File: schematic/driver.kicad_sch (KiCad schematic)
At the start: 14 parts, among them U2 PC817, U3 BUK9K52-60E, U4 BUK9K52-60E, U6 PC817, U7 PC817, U8 PC817

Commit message: a
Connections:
- net Vdrive: now also U2.4
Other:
- title: (none) -> Peltier Driver
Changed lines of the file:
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@@
 (kicad_sch (version 20211123) (generator eeschema)
   (paper "A4")
+  (title_block
+    (title "Peltier Driver")
+    (date "2022-03-18")
+    (comment 1 "Engineer/Draftsman: Joesphan Lu")
+  )
   (junction (at 154.94 57.15) (diameter 0) (color 0 0 0 0)
   )
@@
     (stroke (width 0) (type default) (color 0 0 0 0))
   )
-  (wire (pts (xy 120.65 77.47) (xy 120.65 80.01))
+  (wire (pts (xy 120.65 74.93) (xy 120.65 80.01))
     (stroke (width 0) (type default) (color 0 0 0 0))
   )
@@
     (pin "2")
   )
+  (symbol (lib_id "power:Vdrive") (at 120.65 74.93 0) (mirror y) (unit 1)
+    (in_bom yes) (on_board yes) (fields_autoplaced)
+    (property "Reference" "#PWR?" (id 0) (at 125.73 78.74 0)
+      (effects (font (size 1.27 1.27)) hide)
+    )
+    (property "Value" "Vdrive" (id 1) (at 120.65 71.3542 0))
+    (property "Footprint" "" (id 2) (at 120.65 74.93 0)
+      (effects (font (size 1.27 1.27)) hide)
+    )
+    (property "Datasheet" "" (id 3) (at 120.65 74.93 0)
+      (effects (font (size 1.27 1.27)) hide)
+    )
+    (pin "1")
+  )
   (symbol (lib_id "Device:R") (at 97.79 99.06 270) (unit 1)

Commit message: e
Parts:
- removed C11, C9: 10uF, Capacitor_SMD:C_0805_2012Metric_Pad1.18x1.45mm_HandSolder, symbol Device:C
- removed D1, D2: LL4148, Diode_SMD:D_MiniMELF, symbol Diode:LL4148
- removed R10, R2, R3: 300, Resistor_SMD:R_0805_2012Metric_Pad1.20x1.40mm_HandSolder, symbol Device:R
- removed U2, U6, U7: PC817, Package_SO:SOP-4_3.8x4.1mm_P2.54mm, symbol Isolator:PC817
- added D?: ZMM3V9, Diode_SMD:D_MiniMELF, symbol Diode:ZMMxx
- added R? (x2): 300, Resistor_SMD:R_0805_2012Metric_Pad1.20x1.40mm_HandSolder, symbol Device:R
- added U? (x2): PC817, Package_DIP:DIP-4_W7.62mm, symbol Isolator:PC817
- added U? (x3): NL17SZ14, Package_TO_SOT_SMD:SOT-553, symbol 1KicadLib:NL17SZ14
- added U?: slg55021, symbol 1KicadLib:slg55021
- U8: footprint Package_SO:SOP-4_3.8x4.1mm_P2.54mm -> Package_DIP:DIP-4_W7.62mm
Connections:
- net DRIVER_N: now also R?.2
- net GND: now also U?.2, U?.2, U?.4 (GND)
- net PELTIER_P: now also U?.6 (S)
- net VCC: now also U?.5 (D)
- net Vdrive: now also U?.4, U?.4
- net at U3.4 (G): now also U?.4 (Y)
- net at U3.2 (G): now also D?.2 (A)
- new net: R?.1, U?.1 (x2)
- new net: D?.1 (K), U?.7 (G)
- new net +5V: U?.1 (VCC)
- new net S1_PG: U?.8 (PG)
- new net ~DRIVER_DIR: U?.2 (A), U?.2 (A), U?.2 (ON)
- new net ~DRIVER_EN: U?.3 (SHDN#)

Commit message: d
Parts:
- removed R11, R? (x2): 300, Resistor_SMD:R_0805_2012Metric_Pad1.20x1.40mm_HandSolder, symbol Device:R
- removed U8, U? (x2): PC817, Package_DIP:DIP-4_W7.62mm, symbol Isolator:PC817
- added D2: (no value), Diode_SMD:D_MiniMELF, symbol Diode:ZMMxx
- added J1: (no value), symbol Connector:Conn_01x02_Female
- added U18: (no value), 1kicadlib:TDFN_8_2x2mm_EP_0.9x1.65mm, symbol 1KicadLib:slg55021
- D1: renamed from D?; value ZMM3V9 -> (none)
- U2, U7, U8: renamed from U?; value NL17SZ14 -> (none)
- U3, U4: value BUK9K52-60E -> (none); footprint 1KicadLib:LFPAK56D -> (none); symbol schematic-rescue:BUK9K52-60E-1KicadLib -> 1KicadLib:BUK9K52-60E
- U6: renamed from U?; value slg55021 -> (none); footprint (none) -> 1kicadlib:TDFN_8_2x2mm_EP_0.9x1.65mm
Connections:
- net +5V: now also U2.5 (VCC), U7.5 (VCC), U8.5 (VCC), U18.1 (VCC)
- net GND: now also U2.3 (GND), U7.3 (GND), U8.3 (GND), U18.4 (GND)
- net VCC: now also U18.5 (D)
- net ~DRIVER_EN: now also U18.3 (SHDN#)
- net at U4.4 (G): now also U8.2 (A)
- net at U4.2 (G): now also D2.2 (A)
- net at U8.4 (Y): now also U7.4 (Y), U18.2 (ON)
- net PELTIER_N: no longer names the net of U4.1 (S), U4.5 (D), U4.6 (D)
- net PELTIER_N: now also J1.1 (Pin_1), U18.6 (S)
- net PELTIER_P: no longer names the net of U3.1 (S), U3.5 (D), U3.6 (D), U6.6 (S)
- net PELTIER_P: now also J1.2 (Pin_2)
- net S1_PG: no longer names the net of U6.8 (PG)
- new net: D2.1 (K), U18.7 (G)
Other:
- moved on the sheet: U2, U7, U8

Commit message: d
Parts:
- D1, D2: value (none) -> ZMM3V9
- J1: value (none) -> Peltier Connection; footprint (none) -> Connector_PinHeader_2.54mm:PinHeader_1x02_P2.54mm_Vertical
- U18, U6: value (none) -> slg55021; footprint 1kicadlib:TDFN_8_2x2mm_EP_0.9x1.65mm -> 1KicadLib:TDFN_8_2x2mm_EP_0.9x1.65mm
- U2, U7, U8: value (none) -> NL17SZ14
- U3, U4: value (none) -> BUK9K52-60E; footprint (none) -> 1KicadLib:LFPAK56D
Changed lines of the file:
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@@
       (effects (font (size 1.27 1.27)) (justify left))
     )
-    (property "Value" "" (id 1) (at 129.6416 109.728 0)
-      (effects (font (size 1.27 1.27)) (justify left))
-    )
-    (property "Footprint" "" (id 2) (at 127 107.95 0)
+    (property "Value" "BUK9K52-60E" (id 1) (at 129.6416 109.728 0)
+      (effects (font (size 1.27 1.27)) (justify left))
+    )
+    (property "Footprint" "1KicadLib:LFPAK56D" (id 2) (at 127 107.95 0)
       (effects (font (size 1.27 1.27)) hide)
     )
     (property "Datasheet" "" (id 3) (at 127 107.95 0)
+      (effects (font (size 1.27 1.27)) hide)
+    )
+    (pin "3")
+    (pin "4")
+    (pin "5")
+    (pin "6")
+  )
+  (symbol (lib_id "1KicadLib:BUK9K52-60E") (at 172.72 107.95 0) (mirror y) (unit 2)
+    (in_bom yes) (on_board yes)
+    (property "Reference" "U4" (id 0) (at 170.053 107.4166 0)
+      (effects (font (size 1.27 1.27)) (justify left))
+    )
+    (property "Value" "BUK9K52-60E" (id 1) (at 170.053 109.728 0)
+      (effects (font (size 1.27 1.27)) (justify left))
+    )
+    (property "Footprint" "1KicadLib:LFPAK56D" (id 2) (at 172.72 107.95 0)
+      (effects (font (size 1.27 1.27)) hide)
+    )
+    (property "Datasheet" "" (id 3) (at 172.72 107.95 0)
+      (effects (font (size 1.27 1.27)) hide)
+    )
+    (pin "3")
+    (pin "4")
+    (pin "5")
+    (pin "6")
+  )
+  (symbol (lib_id "1KicadLib:BUK9K52-60E") (at 172.72 90.17 0) (mirror y) (unit 1)
+    (in_bom yes) (on_board yes)
+    (property "Reference" "U4" (id 0) (at 170.053 89.6366 0)
+      (effects (font (size 1.27 1.27)) (justify left))
+    )
+    (property "Value" "BUK9K52-60E" (id 1) (at 170.053 91.948 0)
+      (effects (font (size 1.27 1.27)) (justify left))
+    )
+    (property "Footprint" "1KicadLib:LFPAK56D" (id 2) (at 172.72 90.17 0)
+      (effects (font (size 1.27 1.27)) hide)
+    )
+    (property "Datasheet" "" (id 3) (at 172.72 90.17 0)
       (effects (font (size 1.27 1.27)) hide)
     )
@@
     (pin "7")
     (pin "8")
-    (pin "3")
-    (pin "4")
-    (pin "5")
-    (pin "6")
-  )
-  (symbol (lib_id "1KicadLib:BUK9K52-60E") (at 172.72 107.95 0) (mirror y) (unit 2)
-    (in_bom yes) (on_board yes)
-    (property "Reference" "U4" (id 0) (at 170.053 107.4166 0)
-      (effects (font (size 1.27 1.27)) (justify left))
-    )
-    (property "Value" "" (id 1) (at 170.053 109.728 0)
-      (effects (font (size 1.27 1.27)) (justify left))
-    )
-    (property "Footprint" "" (id 2) (at 172.72 107.95 0)
-      (effects (font (size 1.27 1.27)) hide)
-    )
-    (property "Datasheet" "" (id 3) (at 172.72 107.95 0)
+  )
+  (symbol (lib_id "1KicadLib:BUK9K52-60E") (at 127 90.17 0) (unit 1)
+    (in_bom yes) (on_board yes)
+    (property "Reference" "U3" (id 0) (at 129.6416 89.6366 0)
+      (effects (font (size 1.27 1.27)) (justify left))
+    )
+    (property "Value" "BUK9K52-60E" (id 1) (at 129.6416 91.948 0)
+      (effects (font (size 1.27 1.27)) (justify left))
+    )
+    (property "Footprint" "1KicadLib:LFPAK56D" (id 2) (at 127 90.17 0)
+      (effects (font (size 1.27 1.27)) hide)
+    )
+    (property "Datasheet" "" (id 3) (at 127 90.17 0)
       (effects (font (size 1.27 1.27)) hide)
     )
@@
     (pin "7")
     (pin "8")
-    (pin "3")
-    (pin "4")
-    (pin "5")
-    (pin "6")
-  )
-  (symbol (lib_id "1KicadLib:BUK9K52-60E") (at 172.72 90.17 0) (mirror y) (unit 1)
-    (in_bom yes) (on_board yes)
-    (property "Reference" "U4" (id 0) (at 170.053 89.6366 0)
-      (effects (font (size 1.27 1.27)) (justify left))
-    )
-    (property "Value" "" (id 1) (at 170.053 91.948 0)
-      (effects (font (size 1.27 1.27)) (justify left))
-    )
-    (property "Footprint" "" (id 2) (at 172.72 90.17 0)
-      (effects (font (size 1.27 1.27)) hide)
-    )
-    (property "Datasheet" "" (id 3) (at 172.72 90.17 0)
-      (effects (font (size 1.27 1.27)) hide)
-    )
-    (pin "1")
-    (pin "2")
-    (pin "7")
-    (pin "8")
-    (pin "3")
-    (pin "4")
-    (pin "5")
-    (pin "6")
-  )
-  (symbol (lib_id "1KicadLib:BUK9K52-60E") (at 127 90.17 0) (unit 1)
-    (in_bom yes) (on_board yes)
-    (property "Reference" "U3" (id 0) (at 129.6416 89.6366 0)
-      (effects (font (size 1.27 1.27)) (justify left))
-    )
-    (property "Value" "" (id 1) (at 129.6416 91.948 0)
-      (effects (font (size 1.27 1.27)) (justify left))
-    )
-    (property "Footprint" "" (id 2) (at 127 90.17 0)
-      (effects (font (size 1.27 1.27)) hide)
-    )
-    (property "Datasheet" "" (id 3) (at 127 90.17 0)
-      (effects (font (size 1.27 1.27)) hide)
-    )
-    (pin "1")
-    (pin "2")
-    (pin "7")
-    (pin "8")
-    (pin "3")
-    (pin "4")
-    (pin "5")
-    (pin "6")
   )
   (symbol (lib_id "power:VCC") (at 154.94 76.2 0) (unit 1)
@@
       (effects (font (size 1.27 1.27)) (justify left))
     )
-    (property "Value" "" (id 1) (at 165.8112 142.621 0)
-      (effects (font (size 1.27 1.27)) (justify left))
-    )
-    (property "Footprint" "" (id 2) (at 165.1 139.7 0)
+    (property "Value" "Peltier Connection" (id 1) (at 165.8112 142.621 0)
+      (effects (font (size 1.27 1.27)) (justify left))
+    )
+    (property "Footprint" "Connector_PinHeader_2.54mm:PinHeader_1x02_P2.54mm_Vertical" (id 2) (at 165.1 139.7 0)
       (effects (font (size 1.27 1.27)) hide)
     )
@@
     (in_bom yes) (on_board yes)
     (property "Reference" "U8" (id 0) (at 205.74 109.22 0))
-    (property "Value" "" (id 1) (at 209.55 123.19 0))
+    (property "Value" "NL17SZ14" (id 1) (at 209.55 123.19 0))
     (property "Footprint" "Package_TO_SOT_SMD:SOT-553" (id 2) (at 198.12 118.11 0)
       (effects (font (size 1.27 1.27)) hide)
@@
     (in_bom yes) (on_board yes) (fields_autoplaced)
     (property "Reference" "D2" (id 0) (at 187.96 85.2002 0))
-    (property "Value" "" (id 1) (at 187.96 87.7371 0))
+    (property "Value" "ZMM3V9" (id 1) (at 187.96 87.7371 0))
     (property "Footprint" "Diode_SMD:D_MiniMELF" (id 2) (at 187.96 94.615 0)
       (effects (font (size 1.27 1.27)) hide)
@@
     (in_bom yes) (on_board yes) (fields_autoplaced)
     (property "Reference" "D1" (id 0) (at 110.49 85.2002 0))
-    (property "Value" "" (id 1) (at 110.49 87.7371 0))
+    (property "Value" "ZMM3V9" (id 1) (at 110.49 87.7371 0))
     (property "Footprint" "Diode_SMD:D_MiniMELF" (id 2) (at 110.49 94.615 0)
       (effects (font (size 1.27 1.27)) hide)
@@
     (in_bom yes) (on_board yes)
     (property "Reference" "U7" (id 0) (at 153.67 43.18 0))
-    (property "Value" "" (id 1) (at 157.48 57.15 0))
+    (property "Value" "NL17SZ14" (id 1) (at 157.48 57.15 0))
     (property "Footprint" "Package_TO_SOT_SMD:SOT-553" (id 2) (at 146.05 52.07 0)
       (effects (font (size 1.27 1.27)) hide)
@@
     (in_bom yes) (on_board yes) (fields_autoplaced)
     (property "Reference" "U18" (id 0) (at 208.28 81.441 0))
-    (property "Value" "" (id 1) (at 208.28 83.9779 0))
-    (property "Footprint" "1kicadlib:TDFN_8_2x2mm_EP_0.9x1.65mm" (id 2) (at 207.01 90.17 0)
+    (property "Value" "slg55021" (id 1) (at 208.28 83.9779 0))
+    (property "Footprint" "1KicadLib:TDFN_8_2x2mm_EP_0.9x1.65mm" (id 2) (at 207.01 90.17 0)
       (effects (font (size 1.27 1.27)) hide)
     )
@@
     (in_bom yes) (on_board yes) (fields_autoplaced)
     (property "Reference" "U6" (id 0) (at 90.17 81.441 0))
-    (property "Value" "" (id 1) (at 90.17 83.9779 0))
-    (property "Footprint" "1kicadlib:TDFN_8_2x2mm_EP_0.9x1.65mm" (id 2) (at 91.44 90.17 0)
+    (property "Value" "slg55021" (id 1) (at 90.17 83.9779 0))
+    (property "Footprint" "1KicadLib:TDFN_8_2x2mm_EP_0.9x1.65mm" (id 2) (at 91.44 90.17 0)
       (effects (font (size 1.27 1.27)) hide)
     )
@@
     (in_bom yes) (on_board yes)
     (property "Reference" "U2" (id 0) (at 93.98 109.22 0))
-    (property "Value" "" (id 1) (at 97.79 123.19 0))
+    (property "Value" "NL17SZ14" (id 1) (at 97.79 123.19 0))
     (property "Footprint" "Package_TO_SOT_SMD:SOT-553" (id 2) (at 86.36 118.11 0)
       (effects (font (size 1.27 1.27)) hide)

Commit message: e
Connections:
- net at U4.4 (G): now also U8.4 (Y); no longer U8.2 (A)
- net at U18.2 (ON), U7.4 (Y): now also U8.2 (A); no longer U8.4 (Y)
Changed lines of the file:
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@@
       (effects (font (size 1.27 1.27)) hide)
     )
+    (pin "1")
+    (pin "2")
+    (pin "7")
+    (pin "8")
     (pin "3")
     (pin "4")
@@
       (effects (font (size 1.27 1.27)) hide)
     )
+    (pin "1")
+    (pin "2")
+    (pin "7")
+    (pin "8")
     (pin "3")
     (pin "4")
@@
     (pin "7")
     (pin "8")
+    (pin "3")
+    (pin "4")
+    (pin "5")
+    (pin "6")
   )
   (symbol (lib_id "1KicadLib:BUK9K52-60E") (at 127 90.17 0) (unit 1)
@@
     (pin "7")
     (pin "8")
+    (pin "3")
+    (pin "4")
+    (pin "5")
+    (pin "6")
   )
   (symbol (lib_id "power:VCC") (at 154.94 76.2 0) (unit 1)
@@
     (pin "2")
   )
-  (symbol (lib_id "1KicadLib:NL17SZ14") (at 198.12 118.11 0) (unit 1)
+  (symbol (lib_id "1KicadLib:NL17SZ14") (at 200.66 118.11 0) (mirror y) (unit 1)
     (in_bom yes) (on_board yes)
-    (property "Reference" "U8" (id 0) (at 205.74 109.22 0))
-    (property "Value" "NL17SZ14" (id 1) (at 209.55 123.19 0))
-    (property "Footprint" "Package_TO_SOT_SMD:SOT-553" (id 2) (at 198.12 118.11 0)
+    (property "Reference" "U8" (id 0) (at 193.04 109.22 0))
+    (property "Value" "NL17SZ14" (id 1) (at 189.23 123.19 0))
+    (property "Footprint" "Package_TO_SOT_SMD:SOT-553" (id 2) (at 200.66 118.11 0)
       (effects (font (size 1.27 1.27)) hide)
     )
-    (property "Datasheet" "" (id 3) (at 198.12 118.11 0)
+    (property "Datasheet" "" (id 3) (at 200.66 118.11 0)
       (effects (font (size 1.27 1.27)) hide)
     )

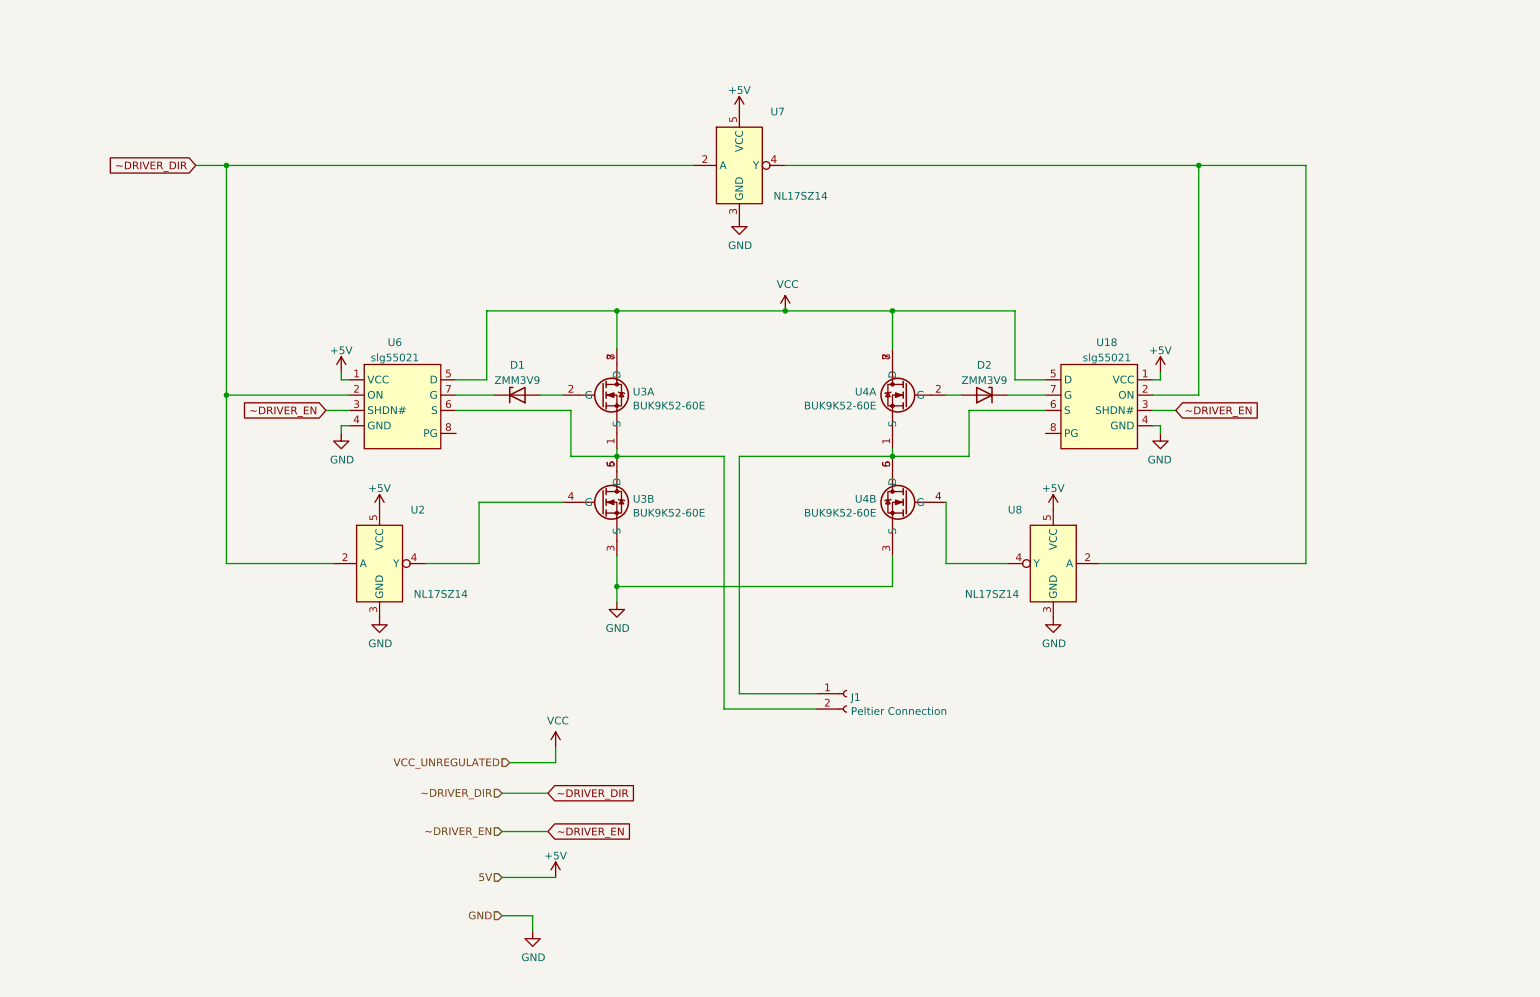
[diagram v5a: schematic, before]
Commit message: beta boards routed
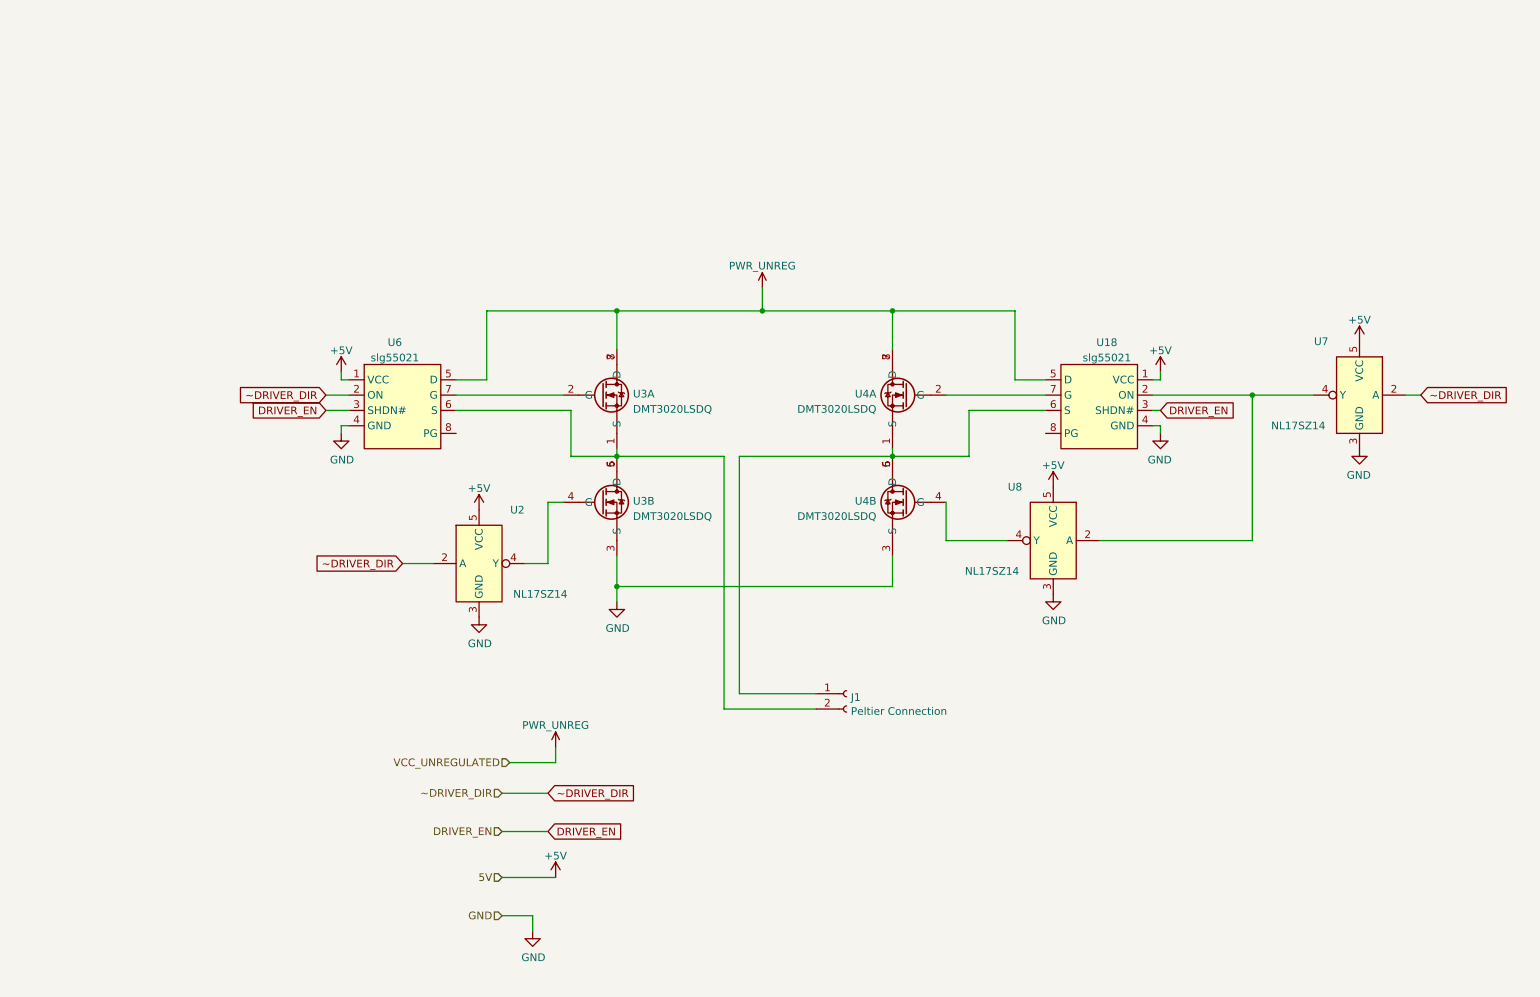
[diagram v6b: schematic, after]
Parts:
- removed D1, D2: ZMM3V9, Diode_SMD:D_MiniMELF, symbol Diode:ZMMxx
- removed U3, U4: BUK9K52-60E, 1KicadLib:LFPAK56D, symbol 1KicadLib:BUK9K52-60E
- added U3, U4: DMT3020LSDQ, Package_SO:SO-8_3.9x4.9mm_P1.27mm, symbol 1KicadLib:DMT3020LSDQ
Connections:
- net GND: now also U3.3 (S), U4.3 (S)
- net at U2.4 (Y): now also U3.4 (G)
- net at J1.2 (Pin_2), U6.6 (S): now also U3.1 (S), U3.5 (D), U3.6 (D)
- net at U8.4 (Y): now also U4.4 (G)
- net at J1.1 (Pin_1), U18.6 (S): now also U4.1 (S), U4.5 (D), U4.6 (D)
- net at U18.7 (G): now also U4.2 (G)
- net at U6.7 (G): now also U3.2 (G)
- net VCC renamed PWR_UNREG
- net PWR_UNREG: now also U3.7 (D), U3.8 (D), U4.7 (D), U4.8 (D)
- net ~DRIVER_EN renamed DRIVER_EN
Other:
- moved on the sheet: U2, U7, U8
